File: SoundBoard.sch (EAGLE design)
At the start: 17 parts, among them IC1 LMV324, U1 ADMP401

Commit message: v2 - updated OPAMP to LM324QT
- rerouted traces to accomodate for new QFN part
- Added electret microphone pins to test both
- rearranged some parts
- increased board dimensions slightly
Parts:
- removed IC1: LMV324, SparkFun-AnalogIC:LMV324
- added Q1: (no value), adafruit:ELECTRET
- added U$1: LMV324QT, LMV324:LMV324QT
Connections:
- net AMP: now also U$1G$2.+IN, U$1G$4.OUT; no longer IC1G3.+IN, IC1G4.OUT
- net GND: now also Q1.1, U$1G$1.-V; no longer IC1G1.-V
- net N$2: now also U$1G$4.-IN; no longer IC1G4.-IN
- net N$3: now also Q1.2
- net N$4: now also U$1G$3.+IN; no longer IC1G2.+IN
- net N$5: now also U$1G$3.-IN; no longer IC1G2.-IN
- net N$6: now also U$1G$2.OUT; no longer IC1G3.OUT
- net N$7: now also U$1G$2.-IN; no longer IC1G3.-IN
- net N$9: now also U$1G$1.+IN; no longer IC1G1.+IN
- net OUT: now also U$1G$3.OUT; no longer IC1G2.OUT
- net VCC: now also U$1G$1.+V; no longer IC1G1.+V
- net VCC/2: now also U$1G$1.-IN, U$1G$1.OUT, U$1G$4.+IN; no longer IC1G1.-IN, IC1G1.OUT, IC1G4.+IN
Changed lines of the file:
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@@
 <?xml version="1.0" encoding="utf-8"?>
 <!DOCTYPE eagle SYSTEM "eagle.dtd">
-<eagle version="8.2.2">
+<eagle version="8.3.0">
 <drawing>
 <settings>
 <setting alwaysvectorfont="no"/>
+<setting keepoldvectorfont="yes"/>
 <setting verticaltext="up"/>
 </settings>
@@
 <part name="R1" library="Adafruit PowerBoost 1000C Rev B" deviceset="MICROBUILDER_RESISTOR" device="_0402MP" value="1K"/>
 <part name="R2" library="Adafruit PowerBoost 1000C Rev B" deviceset="MICROBUILDER_RESISTOR" device="_0402MP" value="10K"/>
-<part name="IC1" library="SparkFun-AnalogIC" deviceset="LMV324" device="" value="LMV324"/>
 <part name="SUPPLY2" library="SparkFun-PowerSymbols" deviceset="VCC" device=""/>
 <part name="GND1" library="supply1" library_urn="urn:adsk.eagle:library:371" deviceset="GND" device=""/>
@@
 <part name="SUPPLY1" library="SparkFun-PowerSymbols" deviceset="VCC" device=""/>
 <part name="GND7" library="supply1" library_urn="urn:adsk.eagle:library:371" deviceset="GND" device=""/>
+<part name="U$1" library="LMV324" deviceset="LMV324QT" device=""/>
+<part name="Q1" library="adafruit" deviceset="ELECTRET" device=""/>
+<part name="GND8" library="supply1" library_urn="urn:adsk.eagle:library:371" deviceset="GND" device=""/>
 </parts>
 <sheets>
@@
 <instance part="R1" gate="G$1" x="-12.7" y="12.7"/>
 <instance part="R2" gate="G$1" x="-33.02" y="20.32" rot="R90"/>
-<instance part="IC1" gate="G1" x="55.88" y="71.12"/>
 <instance part="SUPPLY2" gate="G$1" x="60.96" y="81.28"/>
 <instance part="GND1" gate="1" x="60.96" y="58.42"/>
@@
 <instance part="SUPPLY3" gate="G$1" x="-58.42" y="25.4"/>
 <instance part="SUPPLY4" gate="G$1" x="-33.02" y="27.94"/>
-<instance part="IC1" gate="G3" x="30.48" y="12.7"/>
-<instance part="IC1" gate="G2" x="96.52" y="20.32"/>
 <instance part="D1" gate="G$1" x="53.34" y="12.7"/>
 <instance part="C3" gate="G$1" x="66.04" y="7.62" rot="R180"/>
@@
 <instance part="GND3" gate="1" x="66.04" y="-2.54"/>
 <instance part="GND4" gate="1" x="86.36" y="-5.08"/>
-<instance part="IC1" gate="G4" x="0" y="10.16"/>
 <instance part="R8" gate="G$1" x="45.72" y="81.28" rot="R270"/>
 <instance part="R9" gate="G$1" x="45.72" y="60.96" rot="R270"/>
@@
 <instance part="SUPPLY1" gate="G$1" x="-35.56" y="71.12"/>
 <instance part="GND7" gate="1" x="-35.56" y="58.42"/>
+<instance part="U$1" gate="G$1" x="55.88" y="71.12"/>
+<instance part="U$1" gate="G$2" x="30.48" y="12.7"/>
+<instance part="U$1" gate="G$3" x="96.52" y="20.32"/>
+<instance part="U$1" gate="G$4" x="0" y="10.16"/>
+<instance part="Q1" gate="G$1" x="-48.26" y="-17.78" rot="R180"/>
+<instance part="GND8" gate="1" x="-40.64" y="-22.86"/>
 </instances>
 <busses>
@@
 <wire x1="-5.08" y1="30.48" x2="-5.08" y2="22.86" width="0.1524" layer="91"/>
 <junction x="-5.08" y="22.86"/>
-<pinref part="IC1" gate="G4" pin="-IN"/>
 <wire x1="-5.08" y1="12.7" x2="-2.54" y2="12.7" width="0.1524" layer="91"/>
 <junction x="-5.08" y="12.7"/>
+<pinref part="U$1" gate="G$4" pin="-IN"/>
 </segment>
 </net>
@@
 <wire x1="-33.02" y1="15.24" x2="-33.02" y2="12.7" width="0.1524" layer="91"/>
 <junction x="-33.02" y="12.7"/>
+<wire x1="-35.56" y1="12.7" x2="-35.56" y2="-15.24" width="0.1524" layer="91"/>
+<junction x="-35.56" y="12.7"/>
+<pinref part="Q1" gate="G$1" pin="2"/>
+<wire x1="-35.56" y1="-15.24" x2="-43.18" y2="-15.24" width="0.1524" layer="91"/>
 </segment>
 </net>
@@
 <junction x="17.78" y="22.86"/>
 <wire x1="17.78" y1="10.16" x2="22.86" y2="10.16" width="0.1524" layer="91"/>
-<pinref part="IC1" gate="G3" pin="+IN"/>
 <wire x1="22.86" y1="10.16" x2="27.94" y2="10.16" width="0.1524" layer="91"/>
 <wire x1="22.86" y1="10.16" x2="22.86" y2="7.62" width="0.1524" layer="91"/>
 <junction x="22.86" y="10.16"/>
 <label x="22.86" y="7.62" size="1.778" layer="95" rot="R270" xref="yes"/>
-<pinref part="IC1" gate="G4" pin="OUT"/>
 <wire x1="15.24" y1="10.16" x2="17.78" y2="10.16" width="0.1524" layer="91"/>
 <junction x="17.78" y="10.16"/>
+<pinref part="U$1" gate="G$2" pin="+IN"/>
+<pinref part="U$1" gate="G$4" pin="OUT"/>
 </segment>
 </net>
@@
 </segment>
 <segment>
-<pinref part="IC1" gate="G1" pin="+V"/>
 <wire x1="60.96" y1="78.74" x2="60.96" y2="81.28" width="0.1524" layer="91"/>
 <pinref part="SUPPLY2" gate="G$1" pin="VCC"/>
+<pinref part="U$1" gate="G$1" pin="+V"/>
 </segment>
 <segment>
@@
 </segment>
 <segment>
-<pinref part="IC1" gate="G1" pin="-V"/>
 <wire x1="60.96" y1="63.5" x2="60.96" y2="60.96" width="0.1524" layer="91"/>
 <pinref part="GND1" gate="1" pin="GND"/>
+<pinref part="U$1" gate="G$1" pin="-V"/>
 </segment>
 <segment>
@@
 <pinref part="GND7" gate="1" pin="GND"/>
 </segment>
+<segment>
+<pinref part="Q1" gate="G$1" pin="1"/>
+<wire x1="-43.18" y1="-17.78" x2="-40.64" y2="-17.78" width="0.1524" layer="91"/>
+<wire x1="-40.64" y1="-17.78" x2="-40.64" y2="-20.32" width="0.1524" layer="91"/>
+<pinref part="GND8" gate="1" pin="GND"/>
+</segment>
 </net>
 <net name="N$6" class="0">
 <segment>
-<pinref part="IC1" gate="G3" pin="OUT"/>
 <wire x1="45.72" y1="12.7" x2="50.8" y2="12.7" width="0.1524" layer="91"/>
 <pinref part="D1" gate="G$1" pin="A"/>
+<pinref part="U$1" gate="G$2" pin="OUT"/>
 </segment>
 </net>
@@
 <wire x1="60.96" y1="12.7" x2="60.96" y2="20.32" width="0.1524" layer="91"/>
 <junction x="60.96" y="12.7"/>
-<pinref part="IC1" gate="G3" pin="-IN"/>
 <wire x1="27.94" y1="15.24" x2="25.4" y2="15.24" width="0.1524" layer="91"/>
 <wire x1="25.4" y1="15.24" x2="25.4" y2="20.32" width="0.1524" layer="91"/>
@@
 <wire x1="66.04" y1="12.7" x2="66.04" y2="10.16" width="0.1524" layer="91"/>
 <junction x="66.04" y="12.7"/>
+<pinref part="U$1" gate="G$2" pin="-IN"/>
 </segment>
 </net>
@@
 <wire x1="81.28" y1="12.7" x2="86.36" y2="12.7" width="0.1524" layer="91"/>
 <wire x1="86.36" y1="12.7" x2="86.36" y2="10.16" width="0.1524" layer="91"/>
-<pinref part="IC1" gate="G2" pin="+IN"/>
 <wire x1="93.98" y1="17.78" x2="86.36" y2="17.78" width="0.1524" layer="91"/>
 <wire x1="86.36" y1="17.78" x2="86.36" y2="12.7" width="0.1524" layer="91"/>
 <junction x="86.36" y="12.7"/>
+<pinref part="U$1" gate="G$3" pin="+IN"/>
 </segment>
 </net>
 <net name="N$5" class="0">
 <segment>
-<pinref part="IC1" gate="G2" pin="-IN"/>
 <wire x1="93.98" y1="22.86" x2="88.9" y2="22.86" width="0.1524" layer="91"/>
 <pinref part="R6" gate="G$1" pin="1"/>
@@
 <wire x1="88.9" y1="33.02" x2="96.52" y2="33.02" width="0.1524" layer="91"/>
 <pinref part="R7" gate="G$1" pin="2"/>
+<pinref part="U$1" gate="G$3" pin="-IN"/>
 </segment>
 </net>
@@
 <wire x1="106.68" y1="33.02" x2="116.84" y2="33.02" width="0.1524" layer="91"/>
 <wire x1="116.84" y1="33.02" x2="116.84" y2="20.32" width="0.1524" layer="91"/>
-<pinref part="IC1" gate="G2" pin="OUT"/>
 <wire x1="111.76" y1="20.32" x2="116.84" y2="20.32" width="0.1524" layer="91"/>
 <wire x1="116.84" y1="20.32" x2="121.92" y2="20.32" width="0.1524" layer="91"/>
 <junction x="116.84" y="20.32"/>
 <label x="121.92" y="20.32" size="1.778" layer="95" xref="yes"/>
+<pinref part="U$1" gate="G$3" pin="OUT"/>
 </segment>
 <segment>
@@
 <wire x1="45.72" y1="66.04" x2="45.72" y2="68.58" width="0.1524" layer="91"/>
 <pinref part="R9" gate="G$1" pin="1"/>
-<pinref part="IC1" gate="G1" pin="+IN"/>
 <wire x1="45.72" y1="68.58" x2="45.72" y2="76.2" width="0.1524" layer="91"/>
 <wire x1="53.34" y1="68.58" x2="45.72" y2="68.58" width="0.1524" layer="91"/>
 <junction x="45.72" y="68.58"/>
+<pinref part="U$1" gate="G$1" pin="+IN"/>
 </segment>
 </net>
@@
 <wire x1="73.66" y1="71.12" x2="76.2" y2="71.12" width="0.1524" layer="91"/>
 <label x="76.2" y="71.12" size="1.778" layer="95" xref="yes"/>
-<pinref part="IC1" gate="G1" pin="-IN"/>
 <wire x1="53.34" y1="73.66" x2="50.8" y2="73.66" width="0.1524" layer="91"/>
-<pinref part="IC1" gate="G1" pin="OUT"/>
 <wire x1="71.12" y1="71.12" x2="73.66" y2="71.12" width="0.1524" layer="91"/>
 <junction x="73.66" y="71.12"/>
+<pinref part="U$1" gate="G$1" pin="-IN"/>
+<pinref part="U$1" gate="G$1" pin="OUT"/>
 </segment>
 <segment>
 <wire x1="-5.08" y1="7.62" x2="-5.08" y2="5.08" width="0.1524" layer="91"/>
 <label x="-5.08" y="5.08" size="1.778" layer="95" rot="R270" xref="yes"/>
-<pinref part="IC1" gate="G4" pin="+IN"/>
 <wire x1="-2.54" y1="7.62" x2="-5.08" y2="7.62" width="0.1524" layer="91"/>
+<pinref part="U$1" gate="G$4" pin="+IN"/>
 </segment>
 <segment>
@@
 <compatibility>
 <note version="8.2" severity="warning">
-Since Version 8.2, Eagle supports online libraries. The ids
+Since Version 8.2, EAGLE supports online libraries. The ids
 of those online libraries will not be understood (or retained)
 with this version.

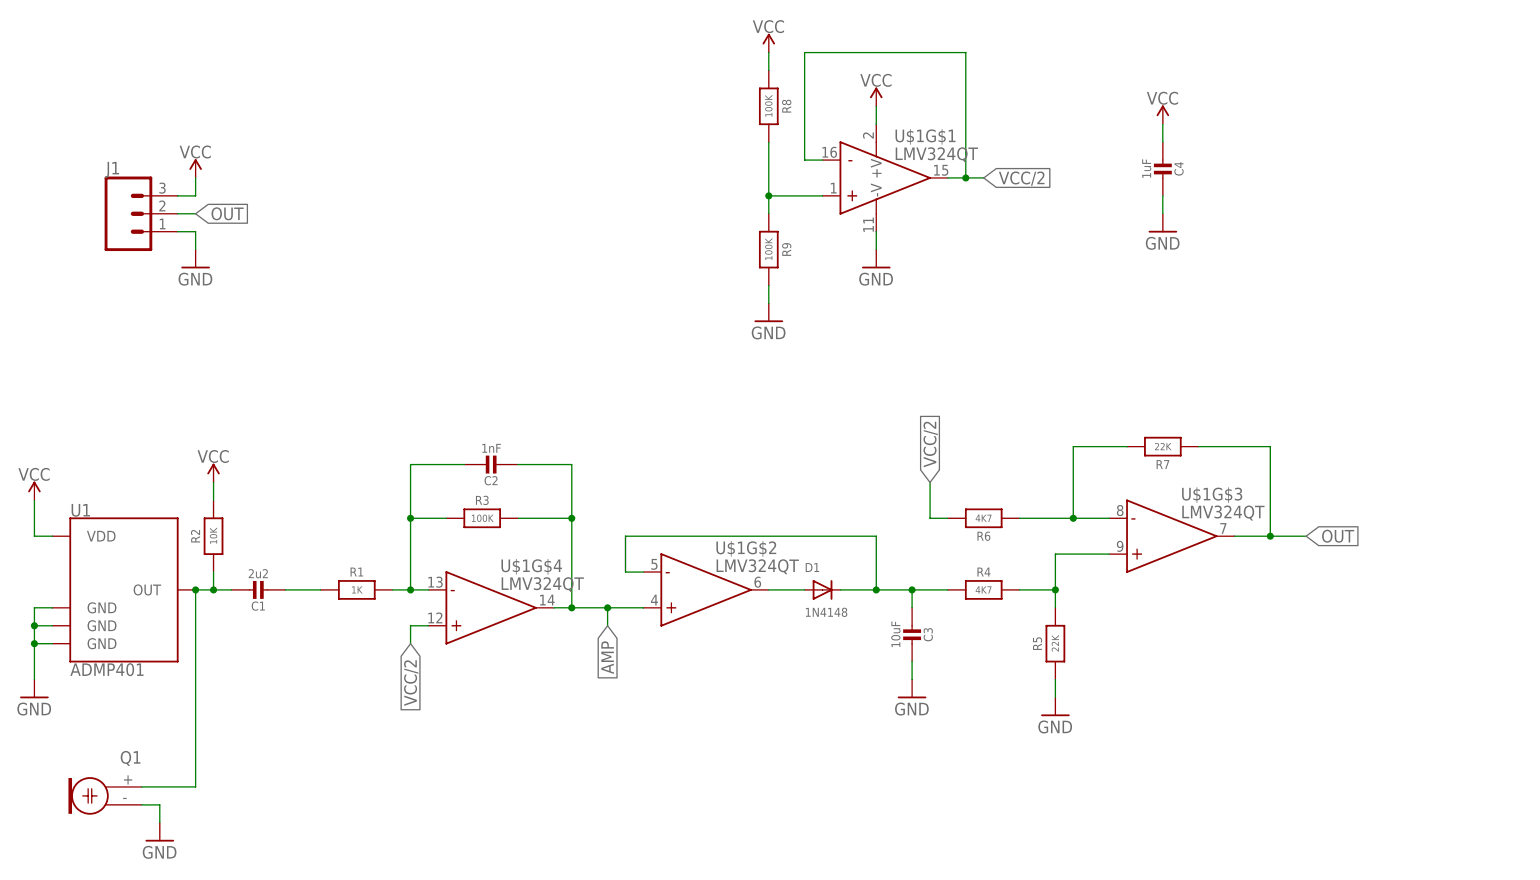
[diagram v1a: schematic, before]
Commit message: v3 - replaced MEMS mic with electret mic (adjusted circuitry)
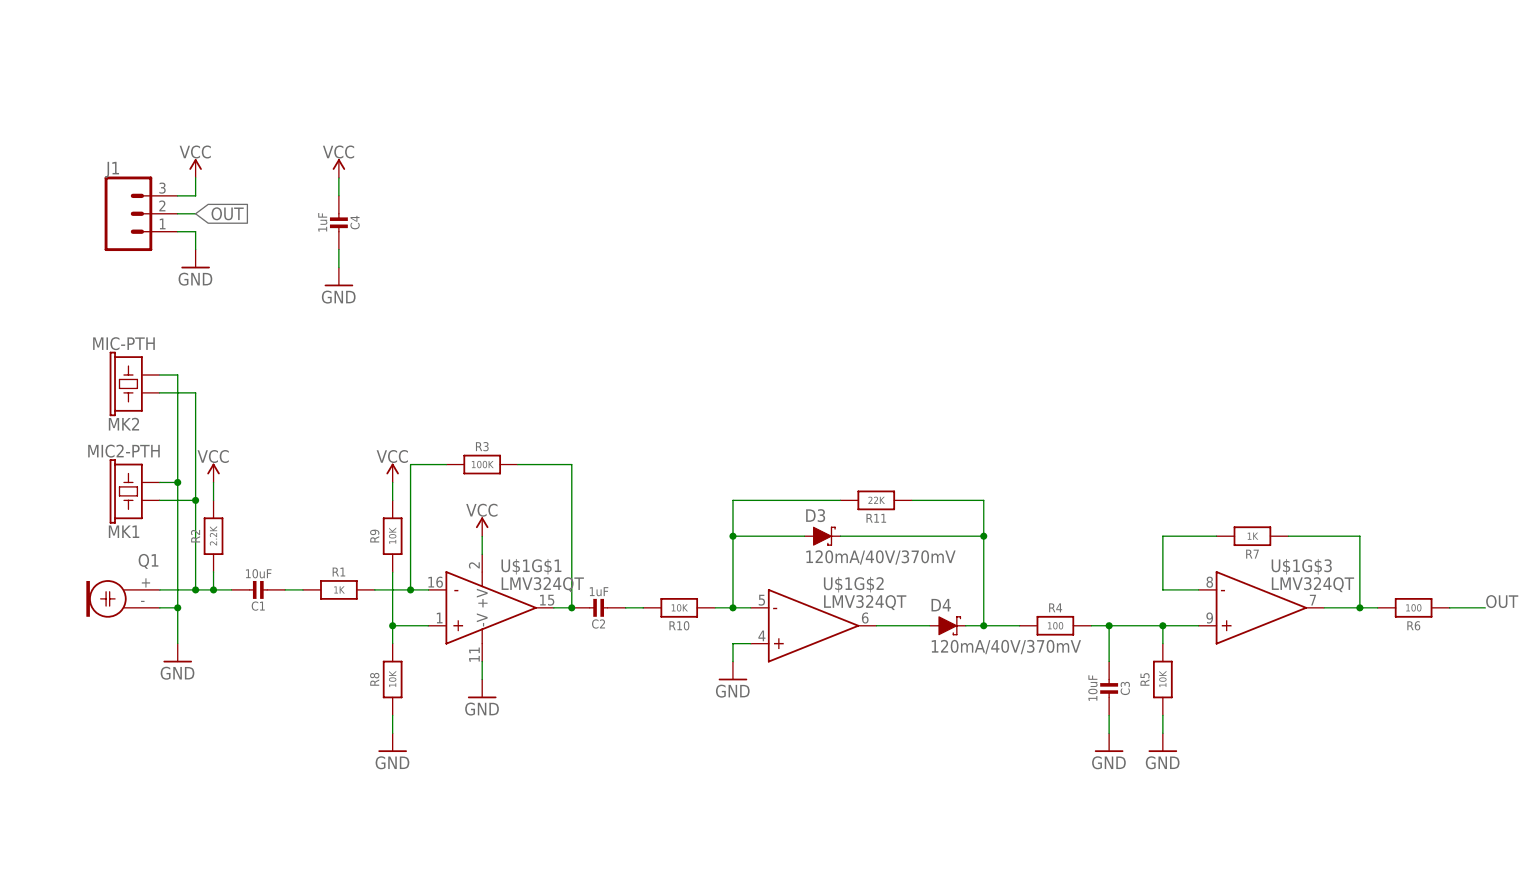
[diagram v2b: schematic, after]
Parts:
- removed D1: 1N4148, adafruit:DIODESOD-123
- removed U1: ADMP401, SparkFun-Sensors:ADMP401
- added D3, D4: 120mA/40V/370mV, SparkFun-DiscreteSemi:DIODE-SCHOTTKY-RB751S40
- added MK1: MIC2-PTH, CMC-4015-40P:MIC2-PTH
- added MK2: MIC-PTH, TOM-1545P-R:MIC-PTH
- added R10: 10K, Adafruit PowerBoost 1000C Rev B:MICROBUILDER_RESISTOR_0402MP
- added R11: 22K, Adafruit PowerBoost 1000C Rev B:MICROBUILDER_RESISTOR_0402MP
- C1: value 2u2 -> 10uF
- C2: value 1nF -> 1uF
- R2: value 10K -> 2.2K
- R4, R6: value 4K7 -> 100
- R5: value 22K -> 10K
- R7: value 22K -> 1K
- R8, R9: value 100K -> 10K
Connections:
- removed net N$3: C1.1, Q1.2, R2.1, U1.OUT
- new net N$10: C1.1, MK1.1, MK2.1, Q1.2, R2.1
- new net N$8: C2.2, R10.2
- new net _OUT: R6.2, R7.1, U$1G$3.OUT
- net AMP: now also C2.1, U$1G$1.OUT; no longer C2.2, U$1G$2.+IN, U$1G$4.OUT
- net GND: now also MK1.2, MK2.2, R8.1, U$1G$2.+IN; no longer R9.2, U1.GND@2, U1.GND@4, U1.GND@6
- net N$2: now also U$1G$1.-IN; no longer C2.1, U$1G$4.-IN
- net N$4: now also D4.A, U$1G$2.OUT; no longer R4.2, R5.2, U$1G$3.+IN
- net N$5: no longer R6.1
- net N$6: now also D3.A, R10.1, R11.2, U$1G$2.-IN; no longer D1.A, U$1G$2.OUT
- net N$7: now also D3.C, D4.C, R11.1; no longer C3.2, D1.C, U$1G$2.-IN
- net N$9: now also C3.2, R4.2, R5.2, U$1G$3.+IN; no longer R8.2, R9.1, U$1G$1.+IN
- net OUT: now also R6.1; no longer R7.1, U$1G$3.OUT
- net VCC: now also R9.2; no longer R8.1, U1.VDD
- net VCC/2: now also R8.2, R9.1, U$1G$1.+IN; no longer R6.2, U$1G$1.-IN, U$1G$1.OUT, U$1G$4.+IN
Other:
- moved on the sheet: C2, C3, C4, Q1, R1, R3, R4, R5, R6, R7, R8, R9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
